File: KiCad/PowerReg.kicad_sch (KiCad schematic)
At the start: 6 parts, among them U1 TPS62162DSG

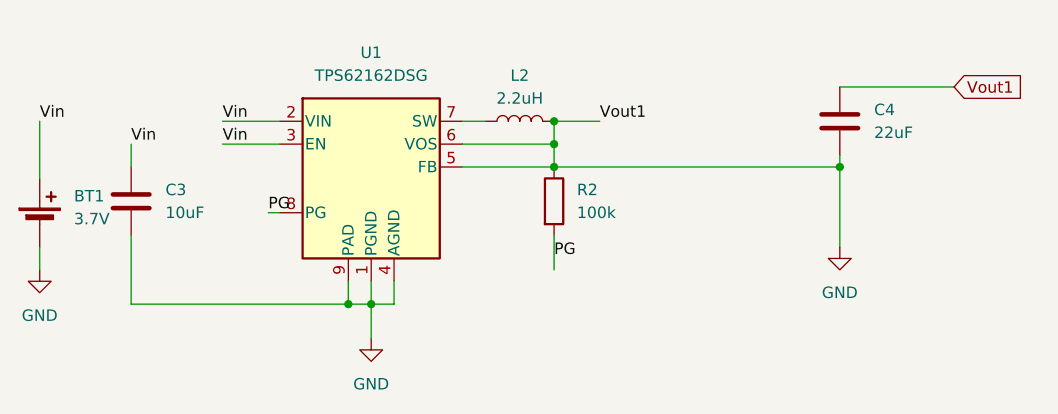
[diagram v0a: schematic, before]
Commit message: Updated base file and added power reg + pyrochannel to main file
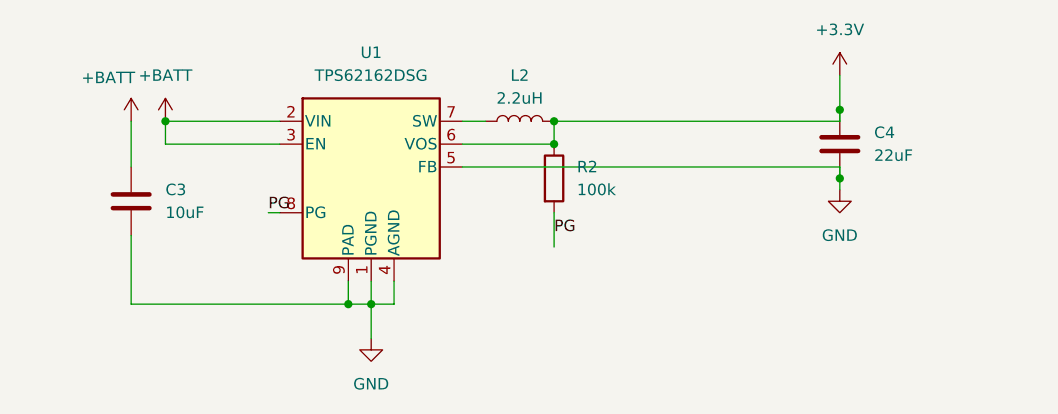
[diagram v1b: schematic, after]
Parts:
- removed BT1: 3.7V, symbol Device:Battery_Cell
- C3, C4: footprint (none) -> Capacitor_SMD:C_0201_0603Metric
- L2: footprint (none) -> Inductor_SMD:L_1008_2520Metric
- R2: footprint (none) -> Resistor_SMD:R_0402_1005Metric
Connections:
- net GND: no longer C4.1, L2.2, R2.1, U1.6 (VOS)
- net Vin renamed +BATT
- new net +3.3V: C4.1, L2.2, R2.1, U1.6 (VOS)
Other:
- moved on the sheet: C4, R2

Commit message: very rough sketch layout
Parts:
- C18: renamed from C3; footprint Capacitor_SMD:C_0201_0603Metric -> Capacitor_SMD:C_0603_1608Metric
- C19: renamed from C4; footprint Capacitor_SMD:C_0201_0603Metric -> Capacitor_SMD:C_0603_1608Metric
- renumbered L2 to L4, R2 to R6, U1 to U2
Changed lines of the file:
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@@
 		(dnp no)
 		(fields_autoplaced yes)
-		(property "Reference" "R2"
+		(property "Reference" "R6"
 			(at 146.05 62.2299 0)
 			(effects
@@
 			(project "PowerReg"
 				(path "/16f8cce7-467e-4342-b55a-00af81cd6f69/bf62daab-1cf5-4742-a85c-ffd3166ecdf9"
-					(reference "R2")
+					(reference "R6")
 					(unit 1)
 				)
@@
 		(dnp no)
 		(fields_autoplaced yes)
-		(property "Reference" "#PWR01"
+		(property "Reference" "#PWR036"
 			(at 175.26 55.88 0)
 			(effects
@@
 			(project ""
 				(path "/16f8cce7-467e-4342-b55a-00af81cd6f69/bf62daab-1cf5-4742-a85c-ffd3166ecdf9"
-					(reference "#PWR01")
+					(reference "#PWR036")
 					(unit 1)
 				)
@@
 		(on_board yes)
 		(dnp no)
-		(property "Reference" "#PWR02"
+		(property "Reference" "#PWR033"
 			(at 96.52 60.96 0)
 			(effects
@@
 			(project ""
 				(path "/16f8cce7-467e-4342-b55a-00af81cd6f69/bf62daab-1cf5-4742-a85c-ffd3166ecdf9"
-					(reference "#PWR02")
+					(reference "#PWR033")
 					(unit 1)
 				)
@@
 		(dnp no)
 		(fields_autoplaced yes)
-		(property "Reference" "U1"
+		(property "Reference" "U2"
 			(at 123.19 49.53 0)
 			(effects
@@
 			(project ""
 				(path "/16f8cce7-467e-4342-b55a-00af81cd6f69/bf62daab-1cf5-4742-a85c-ffd3166ecdf9"
-					(reference "U1")
+					(reference "U2")
 					(unit 1)
 				)
@@
 		(dnp no)
 		(fields_autoplaced yes)
-		(property "Reference" "L2"
+		(property "Reference" "L4"
 			(at 139.7 52.07 90)
 			(effects
@@
 			(project "PowerReg"
 				(path "/16f8cce7-467e-4342-b55a-00af81cd6f69/bf62daab-1cf5-4742-a85c-ffd3166ecdf9"
-					(reference "L2")
+					(reference "L4")
 					(unit 1)
 				)
@@
 		(dnp no)
 		(fields_autoplaced yes)
-		(property "Reference" "C3"
+		(property "Reference" "C18"
 			(at 100.33 64.7699 0)
 			(effects
@@
 			)
 		)
-		(property "Footprint" "Capacitor_SMD:C_0201_0603Metric"
+		(property "Footprint" "Capacitor_SMD:C_0603_1608Metric"
 			(at 97.4852 69.85 0)
 			(effects
@@
 			(project "PowerReg"
 				(path "/16f8cce7-467e-4342-b55a-00af81cd6f69/bf62daab-1cf5-4742-a85c-ffd3166ecdf9"
-					(reference "C3")
+					(reference "C18")
 					(unit 1)
 				)
@@
 		(dnp no)
 		(fields_autoplaced yes)
-		(property "Reference" "#PWR05"
+		(property "Reference" "#PWR037"
 			(at 175.26 71.12 0)
 			(effects
@@
 			(project "PowerReg"
 				(path "/16f8cce7-467e-4342-b55a-00af81cd6f69/bf62daab-1cf5-4742-a85c-ffd3166ecdf9"
-					(reference "#PWR05")
+					(reference "#PWR037")
 					(unit 1)
 				)
@@
 		(dnp no)
 		(fields_autoplaced yes)
-		(property "Reference" "#PWR04"
+		(property "Reference" "#PWR034"
 			(at 100.33 60.96 0)
 			(effects
@@
 			(project ""
 				(path "/16f8cce7-467e-4342-b55a-00af81cd6f69/bf62daab-1cf5-4742-a85c-ffd3166ecdf9"
-					(reference "#PWR04")
+					(reference "#PWR034")
 					(unit 1)
 				)
@@
 		(dnp no)
 		(fields_autoplaced yes)
-		(property "Reference" "C4"
+		(property "Reference" "C19"
 			(at 179.07 58.4199 0)
 			(effects
@@
 			)
 		)
-		(property "Footprint" "Capacitor_SMD:C_0201_0603Metric"
+		(property "Footprint" "Capacitor_SMD:C_0603_1608Metric"
 			(at 176.2252 63.5 0)
 			(effects
@@
 			(project "PowerReg"
 				(path "/16f8cce7-467e-4342-b55a-00af81cd6f69/bf62daab-1cf5-4742-a85c-ffd3166ecdf9"
-					(reference "C4")
+					(reference "C19")
 					(unit 1)
 				)
@@
 		(dnp no)
 		(fields_autoplaced yes)
-		(property "Reference" "#PWR03"
+		(property "Reference" "#PWR035"
 			(at 123.19 87.63 0)
 			(effects
@@
 			(project ""
 				(path "/16f8cce7-467e-4342-b55a-00af81cd6f69/bf62daab-1cf5-4742-a85c-ffd3166ecdf9"
-					(reference "#PWR03")
-					(unit 1)
-				)
+					(reference "#PWR035")
+					(unit 1)
+				)

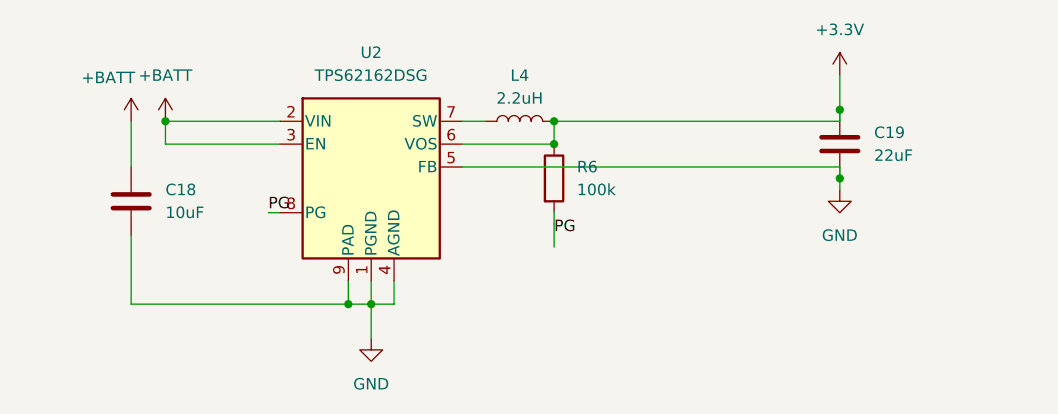
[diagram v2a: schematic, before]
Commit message: redo power regulator area
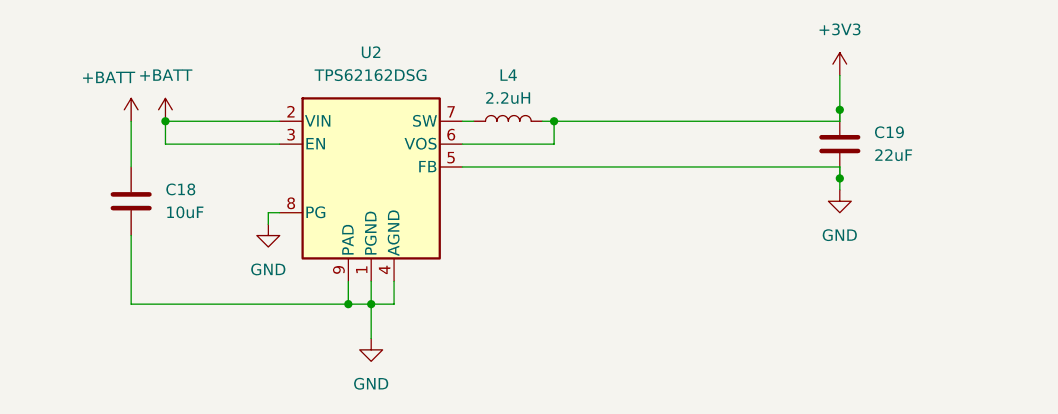
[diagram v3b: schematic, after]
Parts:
- removed R6: 100k, Resistor_SMD:R_0402_1005Metric, symbol Device:R
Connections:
- net PG is gone; now on net GND: U2.8 (PG)
- net +3.3V renamed +3V3
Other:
- moved on the sheet: L4
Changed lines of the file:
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@@
-	)
-	(junction
-		(at 143.51 59.69)
-		(diameter 0)
-		(color 0 0 0 0)
 	)
 	(junction
@@
 	(wire
 		(pts
-			(xy 143.51 71.12) (xy 143.51 67.31)
-		)
-		(stroke
-			(width 0)
-			(type default)
-		)
-	)
-	(wire
-		(pts
 			(xy 123.19 74.93) (xy 123.19 77.47)
 		)
@@
 	(wire
 		(pts
-			(xy 133.35 57.15) (xy 135.89 57.15)
+			(xy 133.35 57.15) (xy 134.62 57.15)
 		)
 		(stroke
@@
 	(wire
 		(pts
-			(xy 111.76 67.31) (xy 113.03 67.31)
+			(xy 142.24 57.15) (xy 143.51 57.15)
 		)
 		(stroke
@@
 	(wire
 		(pts
+			(xy 111.76 67.31) (xy 111.76 68.58)
+		)
+		(stroke
+			(width 0)
+			(type default)
+		)
+	)
+	(wire
+		(pts
 			(xy 96.52 69.85) (xy 96.52 77.47)
 		)
@@
 	(wire
 		(pts
+			(xy 113.03 67.31) (xy 111.76 67.31)
+		)
+		(stroke
+			(width 0)
+			(type default)
+		)
+	)
+	(wire
+		(pts
 			(xy 123.19 77.47) (xy 123.19 81.28)
 		)
@@
 			(width 0)
 			(type default)
-		)
-	)
-	(label "PG"
-		(at 143.51 69.85 0)
-		(effects
-			(font
-				(size 1.27 1.27)
-			)
-			(justify left bottom)
-		)
-	)
-	(label "PG"
-		(at 111.76 67.31 0)
-		(effects
-			(font
-				(size 1.27 1.27)
-			)
-			(justify left bottom)
-		)
-	)
-	(symbol
-		(lib_id "Device:R")
-		(at 143.51 63.5 0)
-		(unit 1)
-		(exclude_from_sim no)
-		(in_bom yes)
-		(on_board yes)
-		(dnp no)
-		(fields_autoplaced yes)
-		(property "Reference" "R6"
-			(at 146.05 62.2299 0)
-			(effects
-				(font
-					(size 1.27 1.27)
-				)
-				(justify left)
-			)
-		)
-		(property "Value" "100k"
-			(at 146.05 64.7699 0)
-			(effects
-				(font
-					(size 1.27 1.27)
-				)
-				(justify left)
-			)
-		)
-		(property "Footprint" "Resistor_SMD:R_0402_1005Metric"
-			(at 141.732 63.5 90)
-			(effects
-				(font
-					(size 1.27 1.27)
-				)
-				(hide yes)
-			)
-		)
-		(property "Datasheet" "~"
-			(at 143.51 63.5 0)
-			(effects
-				(font
-					(size 1.27 1.27)
-				)
-				(hide yes)
-			)
-		)
-		(property "Description" "Resistor"
-			(at 143.51 63.5 0)
-			(effects
-				(font
-					(size 1.27 1.27)
-				)
-				(hide yes)
-			)
-		)
-		(pin "1"
-		)
-		(pin "2"
-		)
-		(instances
-			(project "PowerReg"
-				(path "/16f8cce7-467e-4342-b55a-00af81cd6f69/bf62daab-1cf5-4742-a85c-ffd3166ecdf9"
-					(reference "R6")
-					(unit 1)
-				)
-			)
-			(project "PowerReg"
-				(path "/69b89bc5-ef32-4b14-b574-fcede0ff2705"
-					(reference "R2")
-					(unit 1)
-				)
-			)
-		)
-	)
-	(symbol
-		(lib_id "power:+3.3V")
-		(at 175.26 52.07 0)
-		(unit 1)
-		(exclude_from_sim no)
-		(in_bom yes)
-		(on_board yes)
-		(dnp no)
-		(fields_autoplaced yes)
-		(property "Reference" "#PWR036"
-			(at 175.26 55.88 0)
-			(effects
-				(font
-					(size 1.27 1.27)
-				)
-				(hide yes)
-			)
-		)
-		(property "Value" "+3.3V"
-			(at 175.26 46.99 0)
-			(effects
-				(font
-					(size 1.27 1.27)
-				)
-			)
-		)
-		(property "Footprint" ""
-			(at 175.26 52.07 0)
-			(effects
-				(font
-					(size 1.27 1.27)
-				)
-				(hide yes)
-			)
-		)
-		(property "Datasheet" ""
-			(at 175.26 52.07 0)
-			(effects
-				(font
-					(size 1.27 1.27)
-				)
-				(hide yes)
-			)
-		)
-		(property "Description" "Power symbol creates a global label with name \"+3.3V\""
-			(at 175.26 52.07 0)
-			(effects
-				(font
-					(size 1.27 1.27)
-				)
-				(hide yes)
-			)
-		)
-		(pin "1"
-		)
-		(instances
-			(project ""
-				(path "/16f8cce7-467e-4342-b55a-00af81cd6f69/bf62daab-1cf5-4742-a85c-ffd3166ecdf9"
-					(reference "#PWR036")
-					(unit 1)
-				)
-			)
-			(project ""
-				(path "/69b89bc5-ef32-4b14-b574-fcede0ff2705"
-					(reference "#PWR01")
-					(unit 1)
-				)
-			)
 		)
 	)
@@
 	(symbol
 		(lib_id "Device:L")
-		(at 139.7 57.15 90)
+		(at 138.43 57.15 90)
 		(unit 1)
 		(exclude_from_sim no)
@@
 		(fields_autoplaced yes)
 		(property "Reference" "L4"
-			(at 139.7 52.07 90)
+			(at 138.43 52.07 90)
 			(effects
 				(font
@@
 		)
 		(property "Value" "2.2uH"
-			(at 139.7 54.61 90)
+			(at 138.43 54.61 90)
 			(effects
 				(font
@@
 		)
 		(property "Footprint" "Inductor_SMD:L_1008_2520Metric"
-			(at 139.7 57.15 0)
+			(at 138.43 57.15 0)
 			(effects
 				(font
@@
 		)
 		(property "Datasheet" "~"
-			(at 139.7 57.15 0)
+			(at 138.43 57.15 0)
 			(effects
 				(font
@@
 		)
 		(property "Description" "Inductor"
-			(at 139.7 57.15 0)
+			(at 138.43 57.15 0)
 			(effects
 				(font
@@
 	(symbol
 		(lib_id "power:GND")
+		(at 111.76 68.58 0)
+		(unit 1)
+		(exclude_from_sim no)
+		(in_bom yes)
+		(on_board yes)
+		(dnp no)
+		(fields_autoplaced yes)
+		(property "Reference" "#PWR047"
+			(at 111.76 74.93 0)
+			(effects
+				(font
+					(size 1.27 1.27)
+				)
+				(hide yes)
+			)
+		)
+		(property "Value" "GND"
+			(at 111.76 73.66 0)
+			(effects
+				(font
+					(size 1.27 1.27)
+				)
+			)
+		)
+		(property "Footprint" ""
+			(at 111.76 68.58 0)
+			(effects
+				(font
+					(size 1.27 1.27)
+				)
+				(hide yes)
+			)
+		)
+		(property "Datasheet" ""
+			(at 111.76 68.58 0)
+			(effects
+				(font
+					(size 1.27 1.27)
+				)
+				(hide yes)
+			)
+		)
+		(property "Description" "Power symbol creates a global label with name \"GND\" , ground"
+			(at 111.76 68.58 0)
+			(effects
+				(font
+					(size 1.27 1.27)
+				)
+				(hide yes)
+			)
+		)
+		(pin "1"
+		)
+		(instances
+			(project ""
+				(path "/16f8cce7-467e-4342-b55a-00af81cd6f69/bf62daab-1cf5-4742-a85c-ffd3166ecdf9"
+					(reference "#PWR047")
+					(unit 1)
+				)
+			)
+		)
+	)
+	(symbol
+		(lib_id "power:GND")
 		(at 123.19 81.28 0)
 		(unit 1)
@@
 					(unit 1)
 				)
+			)
+		)
+	)
+	(symbol
+		(lib_id "power:+3V3")
+		(at 175.26 52.07 0)
+		(unit 1)
+		(exclude_from_sim no)
+		(in_bom yes)
+		(on_board yes)
+		(dnp no)
+		(fields_autoplaced yes)
+		(property "Reference" "#PWR036"
+			(at 175.26 55.88 0)
+			(effects
+				(font
+					(size 1.27 1.27)
+				)
+				(hide yes)
+			)
+		)
+		(property "Value" "+3V3"
+			(at 175.26 46.99 0)
+			(effects
+				(font
+					(size 1.27 1.27)
+				)
+			)
+		)
+		(property "Footprint" ""
+			(at 175.26 52.07 0)
+			(effects
+				(font
+					(size 1.27 1.27)
+				)
+				(hide yes)
+			)
+		)
+		(property "Datasheet" ""
+			(at 175.26 52.07 0)
+			(effects
+				(font
+					(size 1.27 1.27)
+				)
+				(hide yes)
+			)
+		)
+		(property "Description" "Power symbol creates a global label with name \"+3V3\""
+			(at 175.26 52.07 0)
+			(effects
+				(font
+					(size 1.27 1.27)
+				)
+				(hide yes)
+			)
+		)
+		(pin "1"
+		)
+		(instances
+			(project ""
+				(path "/16f8cce7-467e-4342-b55a-00af81cd6f69/bf62daab-1cf5-4742-a85c-ffd3166ecdf9"
+					(reference "#PWR036")
+					(unit 1)
+				)
